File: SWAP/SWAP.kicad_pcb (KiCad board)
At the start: 2 copper layers, 58.4 x 26.7 mm, 7 parts, among them J2 Conn_01x08_Male, J3 Conn_01x08_Male, J4 Conn_01x04_Male, U1 74LS573

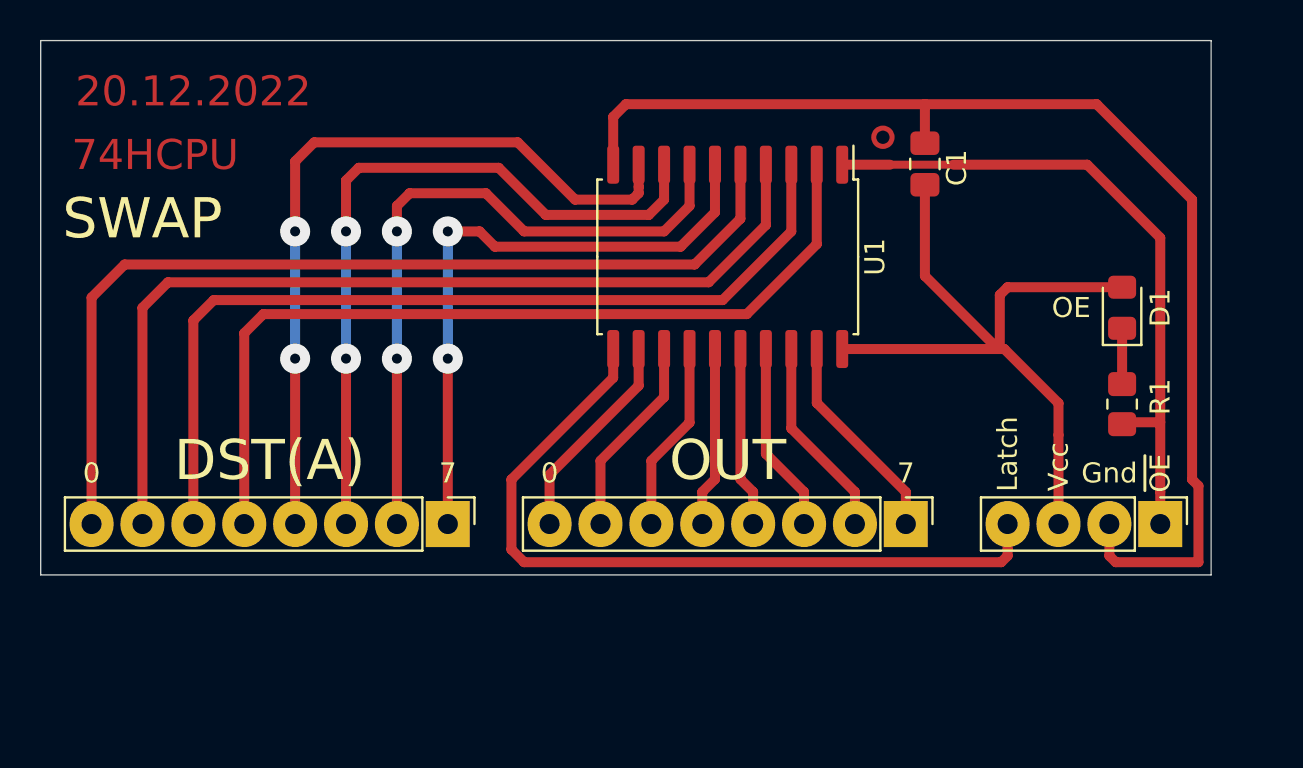
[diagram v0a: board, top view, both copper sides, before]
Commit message: Polishing SWAP cmd
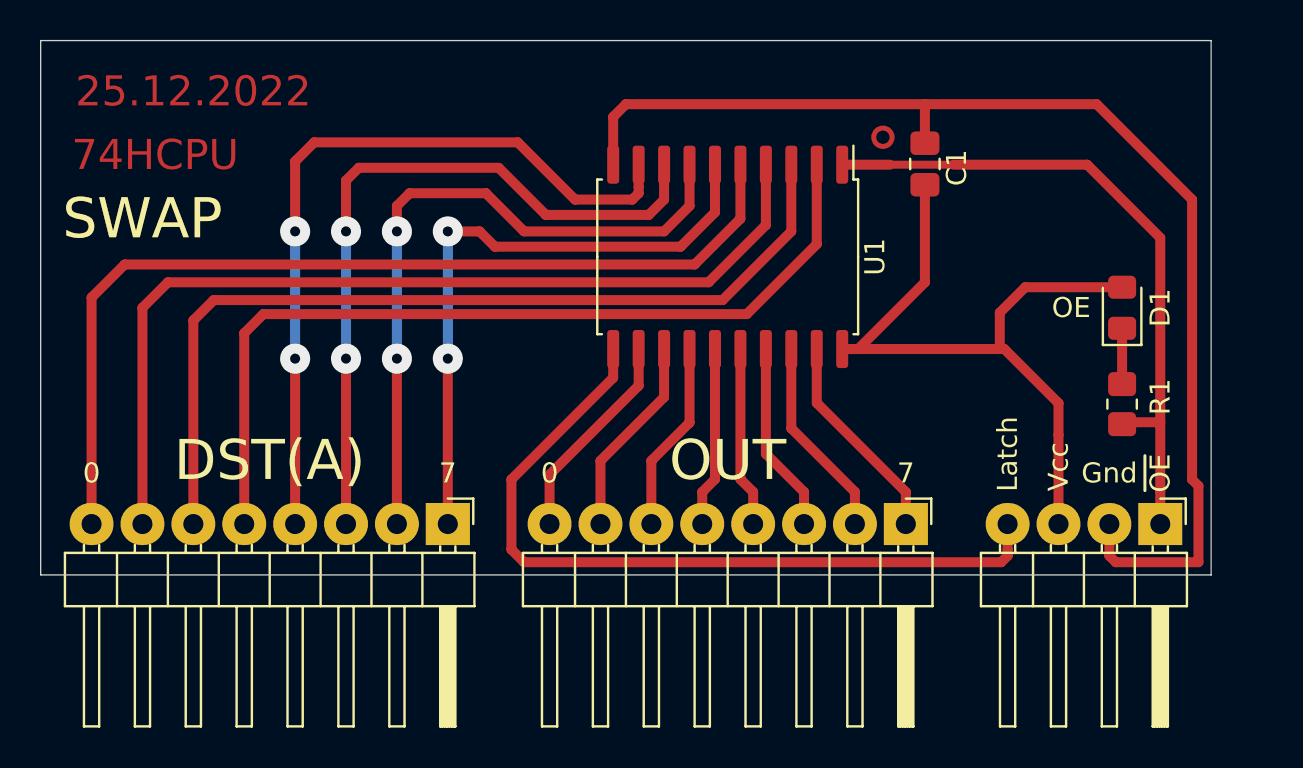
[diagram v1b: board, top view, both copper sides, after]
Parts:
- J2, J3: footprint Connector_PinHeader_2.54mm:PinHeader_1x08_P2.54mm_Vertical -> Connector_PinHeader_2.54mm:PinHeader_1x08_P2.54mm_Horizontal
- J4: footprint Connector_PinHeader_2.54mm:PinHeader_1x04_P2.54mm_Vertical -> Connector_PinHeader_2.54mm:PinHeader_1x04_P2.54mm_Horizontal
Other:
- board text added: "25.12.2022"
- board text removed: "20.12.2022"

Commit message: Set PCB origin
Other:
- board size 58.4 x 26.7 mm -> 61 x 26.7 mm
